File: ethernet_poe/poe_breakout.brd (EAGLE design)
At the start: 47 x 44 mm, 43 parts, among them J1 ARJP11A, U1 W5500, U2 IFX91041, U3 AZ1117EH-3.3TRG1, X1 25MHz

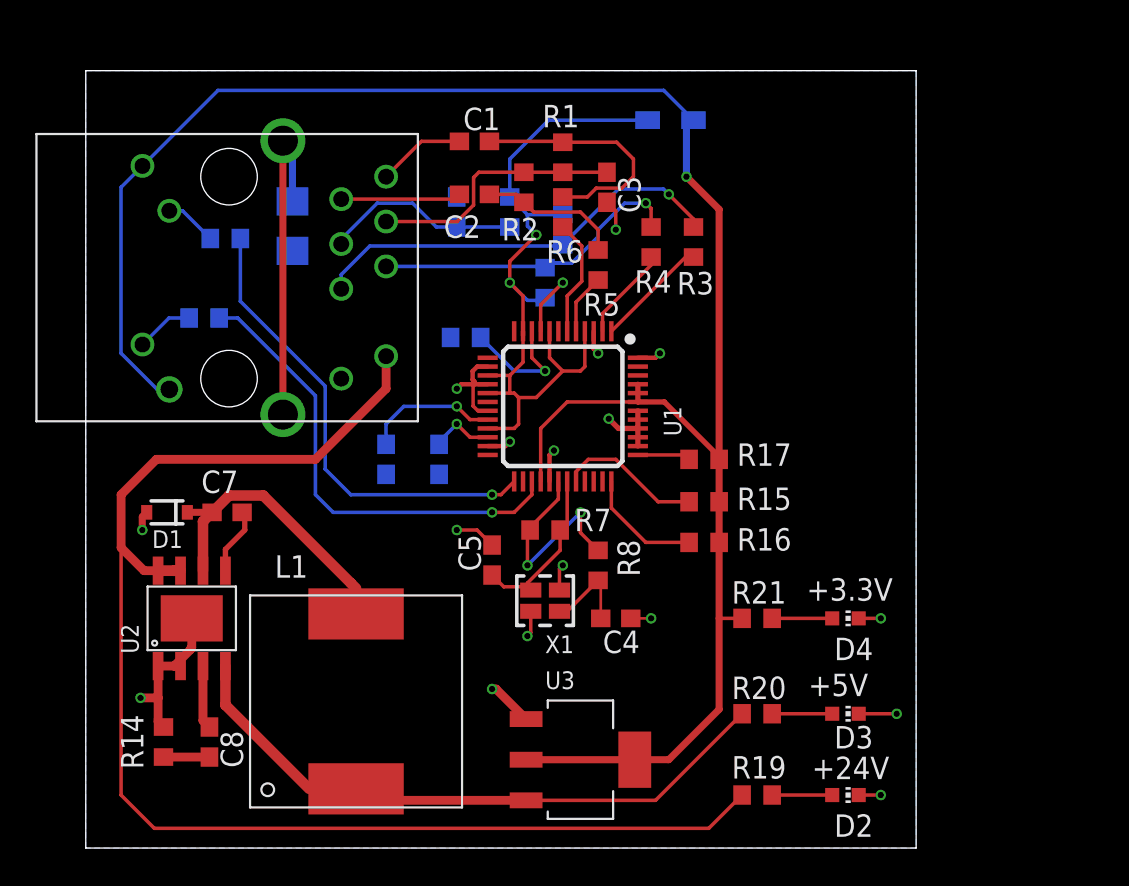
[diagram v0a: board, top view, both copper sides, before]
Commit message: Created design block and breakout board for testing
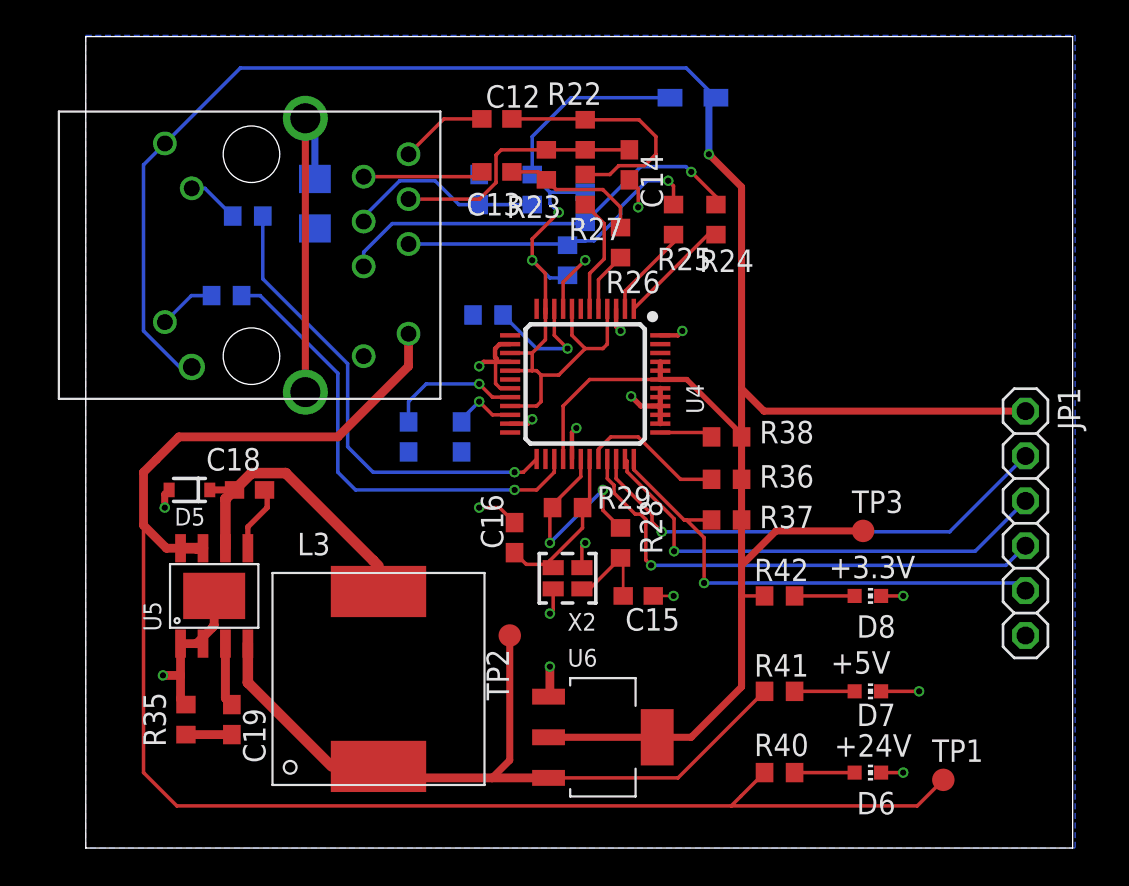
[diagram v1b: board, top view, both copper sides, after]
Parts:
- removed C1, C2, C6: 6.8nF, rcl:C0603
- removed C10, C3: 10nF, rcl:C0603
- removed C11: 1nF/2kV, rcl:C1206
- removed C4, C5: 18pF, rcl:C0603
- removed C7: 220 nF, rcl:C0603
- removed C8: 22 nF, rcl:C0603
- removed C9: 4.7uF, rcl:C0603
- removed D1: (no value), RoboJackets-Diodes:SOD-323
- removed D2, D3, D4: GRN, led:CHIP-LED0603
- removed J1: ARJP11A, ethernet_poe:ARJP11A-MBSB-A-B-EMU2
- removed L1: 47 uH, ethernet_poe:744771147
- removed L2: 742792023, ethernet_poe:0805
- removed R1, R10, R11, R2, R9: 49 1%, rcl:R0603
- removed R12, R13: 330, rcl:R0603
- removed R14: 22k, rcl:R0603
- removed R15, R16, R17: 4.9k, rcl:R0603
- removed R18: 12.4k 1%, rcl:R0603
- removed R19: 4.7k, rcl:R0603
- removed R20: 600, rcl:R0603
- removed R21: 200, rcl:R0603
- removed R3, R4, R5, R6: 33, rcl:R0603
- removed R7: 1M, rcl:R0603
- removed R8: 0, rcl:R0603
- removed U1: W5500, ethernet_poe:48-LQFP
- removed U2: IFX91041, ethernet_poe:SOIC-8-EXPOSED_PAD
- removed U3: AZ1117EH-3.3TRG1, ethernet_poe:SOT230P700X180-4N
- removed X1: 25MHz, ethernet_poe:OSCILLATOR-SMD-2.5X2
- added C12, C13, C17: 6.8nF, rcl:C0603
- added C14, C21: 10nF, rcl:C0603
- added C15, C16: 18pF, rcl:C0603
- added C18: 220 nF, rcl:C0603
- added C19: 22 nF, rcl:C0603
- added C20: 4.7uF, rcl:C0603
- added C22: 1nF/2kV, rcl:C1206
- added D5: (no value), RoboJackets-Diodes:SOD-323
- added D6, D7, D8: GRN, led:CHIP-LED0603
- added J2: ARJP11A, ethernet_poe:ARJP11A-MBSB-A-B-EMU2
- added JP1: (no value), adafruit:1X06
- added L3: 47 uH, ethernet_poe:744771147
- added L4: 742792023, ethernet_poe:0805
- added R22, R23, R30, R31, R32: 49 1%, rcl:R0603
- added R24, R25, R26, R27: 33, rcl:R0603
- added R28: 0, rcl:R0603
- added R29: 1M, rcl:R0603
- added R33, R34: 330, rcl:R0603
- added R35: 22k, rcl:R0603
- added R36, R37, R38: 4.9k, rcl:R0603
- added R39: 12.4k 1%, rcl:R0603
- added R40: 4.7k, rcl:R0603
- added R41: 600, rcl:R0603
- added R42: 200, rcl:R0603
- added TP1, TP2, TP3: TPB1,27, testpad:B1,27
- added U4: W5500, ethernet_poe:48-LQFP
- added U5: IFX91041, ethernet_poe:SOIC-8-EXPOSED_PAD
- added U6: AZ1117EH-3.3TRG1, ethernet_poe:SOT230P700X180-4N
- added X2: 25MHz, ethernet_poe:OSCILLATOR-SMD-2.5X2
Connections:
- removed net 24V_LED: D2.A, R19.2
- removed net 3V3_LED: D4.A, R21.2
- removed net 5V_LED: D3.A, R20.2
- removed net N$10: J1.12, R13.2
- removed net N$11: C5.1, R7.1, U1.31, X1.3
- removed net N$12: J1.13, R12.2
- removed net N$13: R7.2, R8.2, U1.30
- removed net N$14: C7.2, D1.C, L1.P$2, U2.6
- removed net N$15: C7.1, U2.5
- removed net N$16: C8.2, R14.1
- removed net N$17: C8.1, U2.3
- removed net N$18: C10.1, U1.22
- removed net N$19: C9.1, U1.20
- removed net N$21: R18.2, U1.10
- removed net N$4: R3.2, U1.1
- removed net N$5: R4.2, U1.2
- removed net N$7: R5.2, U1.5
- removed net N$8: R6.2, U1.6
- removed net N$9: C4.1, R8.1, X1.1
- removed net RCT: C3.1, J1.3, R1.1, R2.2
- removed net RD+: C1.1, J1.1
- removed net RD-: C2.1, J1.2
- removed net TCT: C6.1, J1.4, R11.1
- new net 24V_LED1: D6.A, R40.2
- new net 3V3_LED1: D8.A, R42.2
- new net 5V_LED1: D7.A, R41.2
- new net N$1: R24.2, U4.1
- new net N$2: R25.2, U4.2
- new net N$20: C15.1, R28.1, X2.1
- new net N$22: R28.2, R29.2, U4.30
- new net N$23: C16.1, R29.1, U4.31, X2.3
- new net N$24: J2.12, R34.2
- new net N$25: J2.13, R33.2
- new net N$26: C18.2, D5.C, L3.P$2, U5.6
- new net N$27: C18.1, U5.5
- new net N$28: C19.2, R35.1
- new net N$29: C19.1, U5.3
- new net N$3: R26.2, U4.5
- new net N$30: C21.1, U4.22
- new net N$31: C20.1, U4.20
- new net N$32: R39.2, U4.10
- new net N$6: R27.2, U4.6
- new net RCT1: C14.1, J2.3, R22.1, R23.2
- new net RD+1: C12.1, J2.1
- new net RD-1: C13.1, J2.2
- new net TCT1: C17.1, J2.4, R32.1
- net !INTN: now also JP1.5, R37.2, U4.36; no longer R16.2, U1.36
- net !RSTN: now also R38.1, U4.37; no longer R17.1, U1.37
- net !SCSN: now also R36.2, U4.32; no longer R15.2, U1.32
- net +24V: now also J2.9, R40.1, TP1.TP, U5.7, U5.8; no longer J1.9, R19.1, U2.7, U2.8
- net +3V3_A: now also L4.1, R30.2, R31.2, R32.2, U4.11, U4.15, U4.17, U4.21, U4.4, U4.8; no longer L2.1, R10.2, R11.2, R9.2, U1.11, U1.15, U1.17, U1.21, U1.4, U1.8
- net +3V3_D: now also J2.11, J2.14, JP1.1, L4.2, R36.1, R37.1, R38.2, R42.1, TP3.TP, U4.28, U4.43, U4.44, U4.45, U6.2, U6.4; no longer J1.11, J1.14, L2.2, R15.1, R16.1, R17.2, R21.1, U1.28, U1.43, U1.44, U1.45, U3.2, U3.4
- net +5V: now also L3.1, R41.1, TP2.TP, U5.4, U6.3; no longer L1.1, R20.1, U2.4, U3.3
- net ACTLED: now also R33.1, U4.27; no longer R12.1, U1.27
- net GND: now also C14.2, C15.2, C16.2, C17.2, C20.2, C21.2, C22.1, D5.A, D6.C, D7.C, D8.C, J2.10, JP1.6, R35.2, R39.1, U4.14, U4.16, U4.19, U4.23, U4.29, U4.3, U4.38, U4.39, U4.40, U4.41, U4.42, U4.48, U4.9, U5.1, U5.2, U5.P$9, U6.1, X2.2, X2.4; no longer C10.2, C11.1, C3.2, C4.2, C5.2, C6.2, C9.2, D1.A, D2.C, D3.C, D4.C, J1.10, R14.2, R18.1, U1.14, U1.16, U1.19, U1.23, U1.29, U1.3, U1.38, U1.39, U1.40, U1.41, U1.42, U1.48, U1.9, U2.1, U2.2, U2.P$9, U3.1, X1.2, X1.4
- net LINKLED: now also R34.1, U4.25; no longer R13.1, U1.25
- net MISO: now also JP1.2, U4.34; no longer U1.34
- net MOSI: now also JP1.3, U4.35; no longer U1.35
- net PE: now also C22.2, J2.15, J2.16; no longer C11.2, J1.15, J1.16
- net RXN: now also C13.2, R23.1, R26.1; no longer C2.2, R2.1, R5.1
- net RXP: now also C12.2, R22.2, R27.1; no longer C1.2, R1.2, R6.1
- net SCLK: now also JP1.4, U4.33; no longer U1.33
- net TXN: now also J2.6, R24.1, R30.1; no longer J1.6, R3.1, R9.1
- net TXP: now also J2.5, R25.1, R31.1; no longer J1.5, R10.1, R4.1
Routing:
- net SCLK: track 0.00 -> 28.9 mm, vias 0 -> 1
- net MISO: track 0.00 -> 27.6 mm, vias 0 -> 1
- net MOSI: track 0.00 -> 27.4 mm, vias 0 -> 1
- net +3V3_D: track 112.2 -> 136.5 mm
- net !INTN: track 6.71 -> 28.7 mm, vias 0 -> 1
- net N$26: track 0.00 -> 17.1 mm
- net N$14: track 17.1 -> 0.00 mm
- net RCT1: track 0.00 -> 14.6 mm
- net RCT: track 14.6 -> 0.00 mm
- net +24V: track 77.8 -> 90.5 mm
- net N$22: track 0.00 -> 12.5 mm, vias 0 -> 2
- net N$13: track 12.5 -> 0.00 mm, vias 2 -> 0
- net TCT: track 11.2 -> 0.00 mm
- net TCT1: track 0.00 -> 11.2 mm
- net N$11: track 9.43 -> 0.00 mm
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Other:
- board size 47 x 44 mm -> 55.9 x 45.9 mm
